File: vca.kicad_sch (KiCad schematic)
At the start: 0 parts

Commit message: modificato:             analog_synth.kicad_pro 	modificato:             fp-info-cache 	nuovo file:             operational.bak 	nuovo file:             operational.kicad_sym 	nuovo file:             sym-lib-table 	nuovo file:             vca.kicad_prl 	modificato:             vca.kicad_sch 	nuovo file:             vcf.kicad_prl
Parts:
- added 12k1: R, symbol Device:R
- added R1, R4, R5, R6, R7: 100k, symbol Device:R
- added R2, R3: 22k, symbol Device:R
- added U1, U2, U3, U5: LM301, symbol Amplifier_Operational:LM301
- added U4: LM1496, Package_DIP:DIP-14_W7.62mm, symbol operational:LM1496
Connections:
- new net: R5.1, R6.1, U5.3 (+)
- new net: R1.2, R2.1, R3.2
- new net: R2.2, R5.2, U4.6 (Output_+)
- new net: R4.2, R7.1, U5.2 (-)
- new net: R7.2, U5.6
- new net: R1.1, U4.5 (Bias)
- new net: R3.1, R4.1, U4.12 (Out_-)
- new net: 12k1.1, U4.2 (Gain_Adj)
- new net: 12k1.2, U4.3 (Gain_Adj)
- new net GNDREF: R6.2

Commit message: modificato:             operational.bak 	modificato:             operational.kicad_sym 	modificato:             vca.kicad_sch
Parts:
- added C1, C5, C6: 4.7uF, symbol Device:C_Polarized_Small
- added C2: 33uF, symbol Device:C_Polarized_Small
- added C3, C4, C7, C8: 33pF, symbol Device:C_Small
- added D1: 1N4148, Diode_THT:D_DO-35_SOD27_P7.62mm_Horizontal, symbol Diode:1N4148
- added R10, R22, R26: 470k, symbol Device:R
- added R11: 8.2k, symbol Device:R
- added R12, R24: 22k, symbol Device:R
- added R13, R14, R16, R17, R18, R21: 12k, symbol Device:R
- added R15: 4.7k, symbol Device:R
- added R19: 3.3m, symbol Device:R
- added R20, R9: 47k, symbol Device:R
- added R23: 10k, symbol Device:R
- added R25, R27: 330, symbol Device:R
- added R28: 3.3k, symbol Device:R
- added RV1: 47k, symbol Device:R_Potentiometer
- added RV2: 10k, symbol Device:R_Potentiometer
- added SW1: SELECTOR, symbol Switch:SW_DPDT_x2
- R8: renamed from 12k1; value R -> 12k
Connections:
- net GNDREF: now also R6.1, U1.3 (+), U3.3 (+), C2.1, R11.2, R25.1, R27.1, RV2.3; no longer R6.2
- net at R2.2, R5.2: now also R3.2; no longer U4.6 (Output_+)
- net at U5.1 (BAL): now also C4.1
- net at R4.2, U5.2 (-): now also R1.2; no longer R7.1
- net -14V: now reaches U5.4 (V-)
- net -14V: now also U1.4 (V-), U2.4 (V-), U3.4 (V-), U4.14 (V__-), R12.1, R19.1, R26.1
- net at R7.2: now also R6.2, U5.3 (+); no longer U5.6
- net +14V: now reaches U5.7 (V+)
- net +14V: now also U1.7 (V+), U2.7 (V+), U3.7 (V+)
- net at U5.8 (C/B): now also C4.2
- net at U3.1 (BAL): now also C7.2
- net at U3.2 (-): now also R20.2, R22.1
- net at U3.6: now also R22.2, R23.1
- net at U3.8 (C/B): now also C7.1
- net at R1.1: now also U5.6, C6.1; no longer U4.5 (Bias)
- net at U1.1 (BAL): now also C3.1
- net at U1.2 (-): now also R10.1, R9.2
- net at U1.6: now also R10.2, R15.1
- net at U1.8 (C/B): now also C3.2
- net at U2.1 (BAL): now also C8.1
- net at U2.2 (-): now also D1.1 (K), R24.1
- net at U2.3 (+): now also R16.2, R17.2, R18.2, R19.2, R21.1
- net at U2.6: now also D1.2 (A)
- net at U2.8 (C/B): now also C8.2
- net at R4.1, U4.12 (Out_-): now also R2.1; no longer R3.1
- net at U4.1 (Signal_In+): now also R14.2, R15.2
- net at U4.10 (Car_In_-): now also U4.8 (Car_In_-), R27.2, RV1.3
- net at U4.4 (Signal_In_-): now also R13.2
- net at U4.7 (Car_In_+): now also R23.2, R24.2, R25.2, RV1.1
- new net: C1.2, R9.1
- new net: R26.2, RV1.2
- new net: R5.1, U4.5 (Bias)
- new net: R3.1, R7.1, U4.6 (Out_+)
- new net: C5.2, R20.1
- new net: C2.2, R11.1, R12.2, R13.1, R14.1
- new net: C6.2, RV2.1
- new net: R28.1, RV2.2
- new net CARRIER_IN: C5.1, SW1.1 (A)
- new net CVOLT_A: SW1.3 (C)
- new net CVOLT_B: R21.2
- new net CVOLT_C: R16.1
- new net CVOLT_D: R17.1
- new net CVOLT_E: R18.1
- new net CVOLT_IN: SW1.2 (B)
- new net OUT_SIGN: R28.2
- new net VCA_IN_SIG: C1.1
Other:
- moved on the sheet: R1, R2, R3, R4, R5, R6, R7, R8, U1, U2, U3, U5

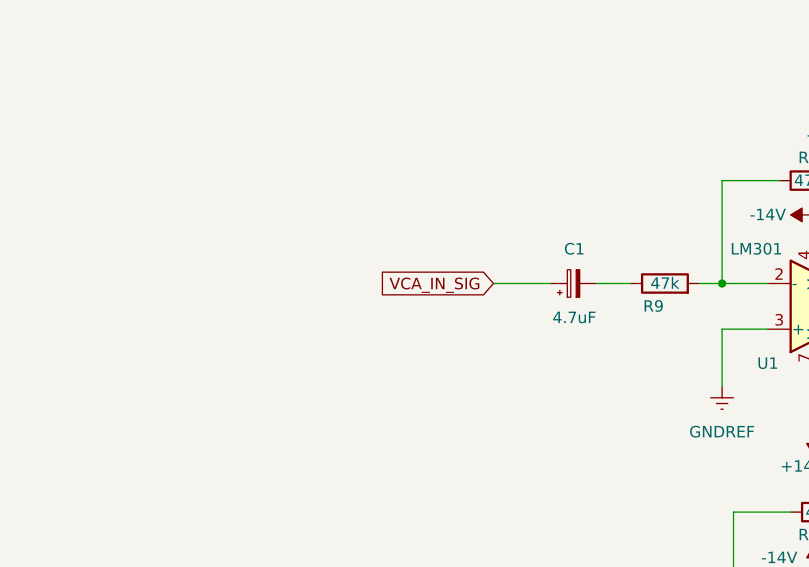
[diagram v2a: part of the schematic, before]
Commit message: modificato:             analog_synth.kicad_pro 	modificato:             key_encoder.kicad_sch 	modificato:             vca.kicad_pro 	modificato:             vca.kicad_sch 	nuovo file:             vca.net 	modificato:             vcf.kicad_sch
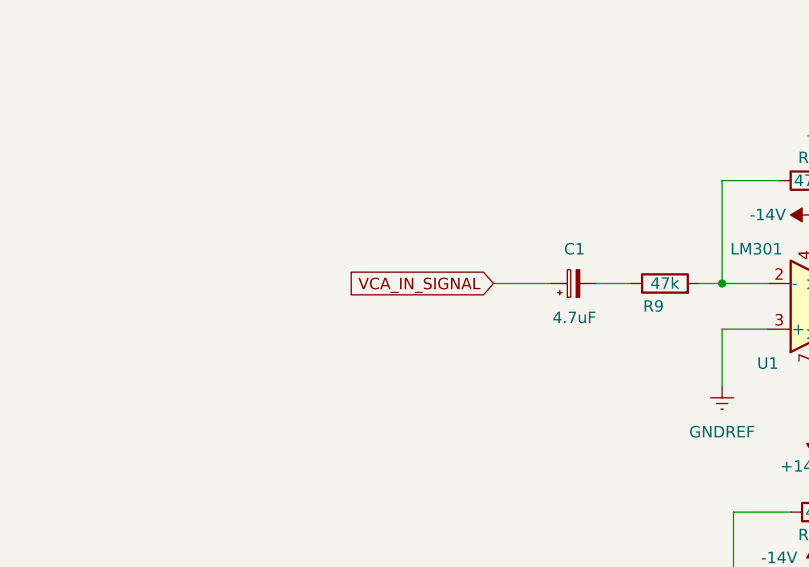
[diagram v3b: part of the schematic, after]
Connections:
- net VCA_IN_SIG renamed VCA_IN_SIGNAL
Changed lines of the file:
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@@
 		)
 	)
-	(global_label "VCA_IN_SIG"
+	(global_label "VCA_IN_SIGNAL"
 		(shape input)
 		(at 127 123.19 180)
@@
 		)
 		(property "Intersheetrefs" "${INTERSHEET_REFS}"
-			(at 113.6128 123.19 0)
+			(at 110.1656 123.19 0)
 			(effects
 				(font

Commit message: eliminato:              adsr.kicad_pcb     eliminato:              adsr.kicad_pro 	modificato:             analog_synth.kicad_pcb 	nuovo file:             analog_synth.net 	eliminato:              audio_mixer.kicad_pcb 	eliminato:              audio_mixer.kicad_pro 	eliminato:              key_encoder.kicad_pcb 	eliminato:              key_encoder.kicad_pro 	modificato:             key_encoder.kicad_sch 	eliminato:              lfo.kicad_pcb 	eliminato:              lfo.kicad_pro 	eliminato:              noise_gen.kicad_pcb 	eliminato:              noise_gen.kicad_pro 	eliminato:              vca.kicad_pcb 	eliminato:              vca.kicad_prl 	eliminato:              vca.kicad_pro 	modificato:             vca.kicad_sch 	eliminato:              vca.net 	eliminato:              vcf.kicad_pcb 	eliminato:              vcf.kicad_prl 	eliminato:              vcf.kicad_pro 	modificato:             vcf.kicad_sch 	eliminato:              vco.kicad_pcb 	eliminato:              vco.kicad_pro
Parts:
- R1, R10, R11, R12, R13, R14, R15, R16, R17, R18, R19, R2, R20, R21, R22, R23, R24, R25, R26, R27, R28, R3, R4, R5, R6, R7, R8, R9, RV1, RV2: footprint (none) -> Resistor_SMD:R_0805_2012Metric
- U1, U2, U3, U5: footprint (none) -> Package_DIP:DIP-8_W7.62mm_Socket
- U4: footprint Package_DIP:DIP-14_W7.62mm -> Package_DIP:DIP-14_W7.62mm_Socket
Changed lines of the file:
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@@
 			)
 		)
-		(property "Footprint" ""
+		(property "Footprint" "Resistor_SMD:R_0805_2012Metric"
 			(at 135.89 188.468 90)
 			(effects
@@
 			)
 		)
-		(property "Footprint" ""
+		(property "Footprint" "Resistor_SMD:R_0805_2012Metric"
 			(at 260.858 104.14 90)
 			(effects
@@
 			)
 		)
-		(property "Footprint" ""
+		(property "Footprint" "Resistor_SMD:R_0805_2012Metric"
 			(at 244.348 74.93 90)
 			(effects
@@
 			)
 		)
-		(property "Footprint" ""
+		(property "Footprint" "Package_DIP:DIP-8_W7.62mm_Socket"
 			(at 270.51 91.44 0)
 			(effects
@@
 			)
 		)
-		(property "Footprint" ""
+		(property "Footprint" "Resistor_SMD:R_0805_2012Metric"
 			(at 216.408 120.65 90)
 			(effects
@@
 			)
 		)
-		(property "Footprint" ""
+		(property "Footprint" "Resistor_SMD:R_0805_2012Metric"
 			(at 211.328 119.38 90)
 			(effects
@@
 			)
 		)
-		(property "Footprint" "Package_DIP:DIP-14_W7.62mm"
+		(property "Footprint" "Package_DIP:DIP-14_W7.62mm_Socket"
 			(at 246.38 107.95 0)
 			(effects
@@
 			)
 		)
-		(property "Footprint" ""
+		(property "Footprint" "Package_DIP:DIP-8_W7.62mm_Socket"
 			(at 166.37 163.83 0)
 			(effects
@@
 			)
 		)
-		(property "Footprint" ""
+		(property "Footprint" "Resistor_SMD:R_0805_2012Metric"
 			(at 221.488 119.38 90)
 			(effects
@@
 			)
 		)
-		(property "Footprint" ""
+		(property "Footprint" "Resistor_SMD:R_0805_2012Metric"
 			(at 147.32 161.798 90)
 			(effects
@@
 			)
 		)
-		(property "Footprint" ""
+		(property "Footprint" "Resistor_SMD:R_0805_2012Metric"
 			(at 182.88 127.508 90)
 			(effects
@@
 			)
 		)
-		(property "Footprint" ""
+		(property "Footprint" "Resistor_SMD:R_0805_2012Metric"
 			(at 267.97 71.882 90)
 			(effects
@@
 			)
 		)
-		(property "Footprint" ""
+		(property "Footprint" "Resistor_SMD:R_0805_2012Metric"
 			(at 182.88 91.948 90)
 			(effects
@@
 			)
 		)
-		(property "Footprint" ""
+		(property "Footprint" "Resistor_SMD:R_0805_2012Metric"
 			(at 135.89 193.548 90)
 			(effects
@@
 			)
 		)
-		(property "Footprint" ""
+		(property "Footprint" "Resistor_SMD:R_0805_2012Metric"
 			(at 135.89 182.118 90)
 			(effects
@@
 			)
 		)
-		(property "Footprint" ""
+		(property "Footprint" "Resistor_SMD:R_0805_2012Metric"
 			(at 182.88 164.338 90)
 			(effects
@@
 			)
 		)
-		(property "Footprint" ""
+		(property "Footprint" "Package_DIP:DIP-8_W7.62mm_Socket"
 			(at 166.37 127 0)
 			(effects
@@
 			)
 		)
-		(property "Footprint" ""
+		(property "Footprint" "Resistor_SMD:R_0805_2012Metric"
 			(at 146.558 204.47 90)
 			(effects
@@
 			)
 		)
-		(property "Footprint" ""
+		(property "Footprint" "Resistor_SMD:R_0805_2012Metric"
 			(at 289.56 115.57 0)
 			(effects
@@
 			)
 		)
-		(property "Footprint" ""
+		(property "Footprint" "Package_DIP:DIP-8_W7.62mm_Socket"
 			(at 167.64 193.04 0)
 			(effects
@@
 			)
 		)
-		(property "Footprint" ""
+		(property "Footprint" "Resistor_SMD:R_0805_2012Metric"
 			(at 248.158 74.93 90)
 			(effects
@@
 			)
 		)
-		(property "Footprint" ""
+		(property "Footprint" "Resistor_SMD:R_0805_2012Metric"
 			(at 154.178 184.15 90)
 			(effects
@@
 			)
 		)
-		(property "Footprint" ""
+		(property "Footprint" "Resistor_SMD:R_0805_2012Metric"
 			(at 252.73 94.488 90)
 			(effects
@@
 			)
 		)
-		(property "Footprint" ""
+		(property "Footprint" "Resistor_SMD:R_0805_2012Metric"
 			(at 201.168 180.34 90)
 			(effects
@@
 			)
 		)
-		(property "Footprint" ""
+		(property "Footprint" "Resistor_SMD:R_0805_2012Metric"
 			(at 252.73 89.408 90)
 			(effects
@@
 			)
 		)
-		(property "Footprint" ""
+		(property "Footprint" "Resistor_SMD:R_0805_2012Metric"
 			(at 163.83 150.368 90)
 			(effects
@@
 			)
 		)
-		(property "Footprint" ""
+		(property "Footprint" "Resistor_SMD:R_0805_2012Metric"
 			(at 229.108 68.58 90)
 			(effects
@@
 			)
 		)
-		(property "Footprint" ""
+		(property "Footprint" "Resistor_SMD:R_0805_2012Metric"
 			(at 166.878 95.25 90)
 			(effects
@@
 			)
 		)
-		(property "Footprint" ""
+		(property "Footprint" "Resistor_SMD:R_0805_2012Metric"
 			(at 162.56 113.538 90)
 			(effects
@@
 			)
 		)
-		(property "Footprint" ""
+		(property "Footprint" "Resistor_SMD:R_0805_2012Metric"
 			(at 219.202 68.58 90)
 			(effects
@@
 			)
 		)
-		(property "Footprint" ""
+		(property "Footprint" "Resistor_SMD:R_0805_2012Metric"
 			(at 182.88 88.138 90)
 			(effects
@@
 			)
 		)
-		(property "Footprint" ""
+		(property "Footprint" "Resistor_SMD:R_0805_2012Metric"
 			(at 302.768 101.6 90)
 			(effects
@@
 			)
 		)
-		(property "Footprint" ""
+		(property "Footprint" "Resistor_SMD:R_0805_2012Metric"
 			(at 166.878 80.01 90)
 			(effects
@@
 			)
 		)
-		(property "Footprint" ""
+		(property "Footprint" "Resistor_SMD:R_0805_2012Metric"
 			(at 214.63 113.03 0)
 			(effects
@@
 			)
 		)
-		(property "Footprint" ""
+		(property "Footprint" "Resistor_SMD:R_0805_2012Metric"
 			(at 146.05 124.968 90)
 			(effects
